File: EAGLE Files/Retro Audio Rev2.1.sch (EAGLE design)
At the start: 72 parts, among them IC1 MAX98357A, Q1 2.5A/30V, Q2 MBT3904DW1T1, Q3 AOD417, SW1 OS102011MA1Q, SW5 PEC11, U2 ESP-WROOM-32, U3 AP2112K-3.3V, U4 FT231XS, X2 19269

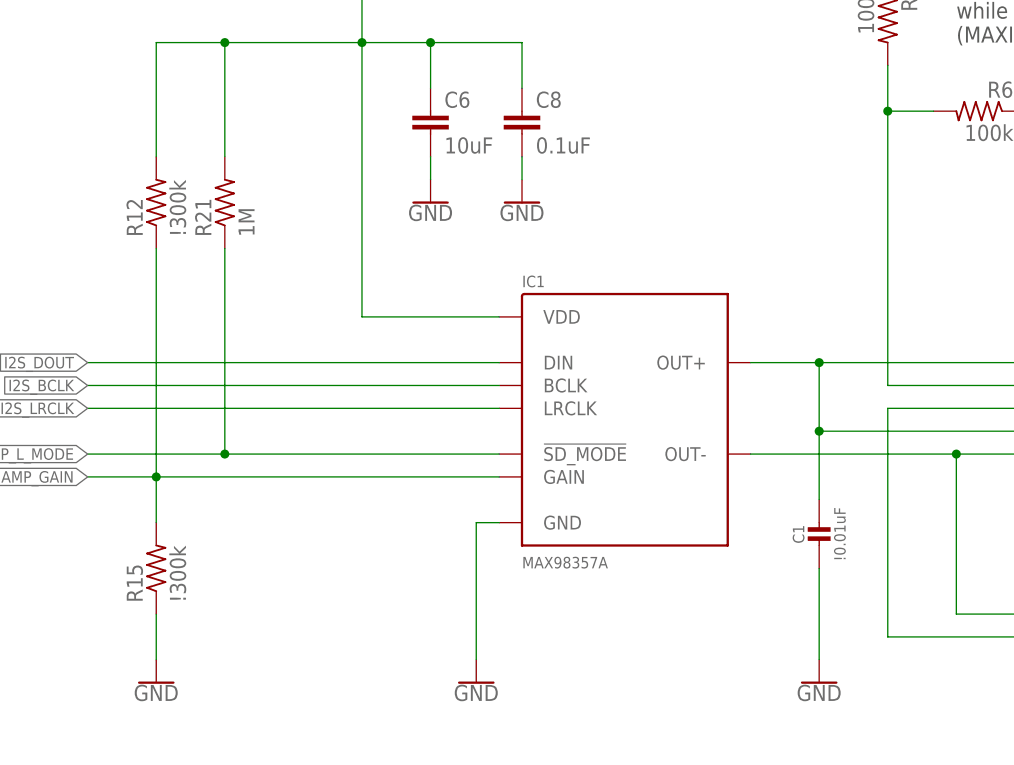
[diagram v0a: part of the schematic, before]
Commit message: Updated to show unused parts
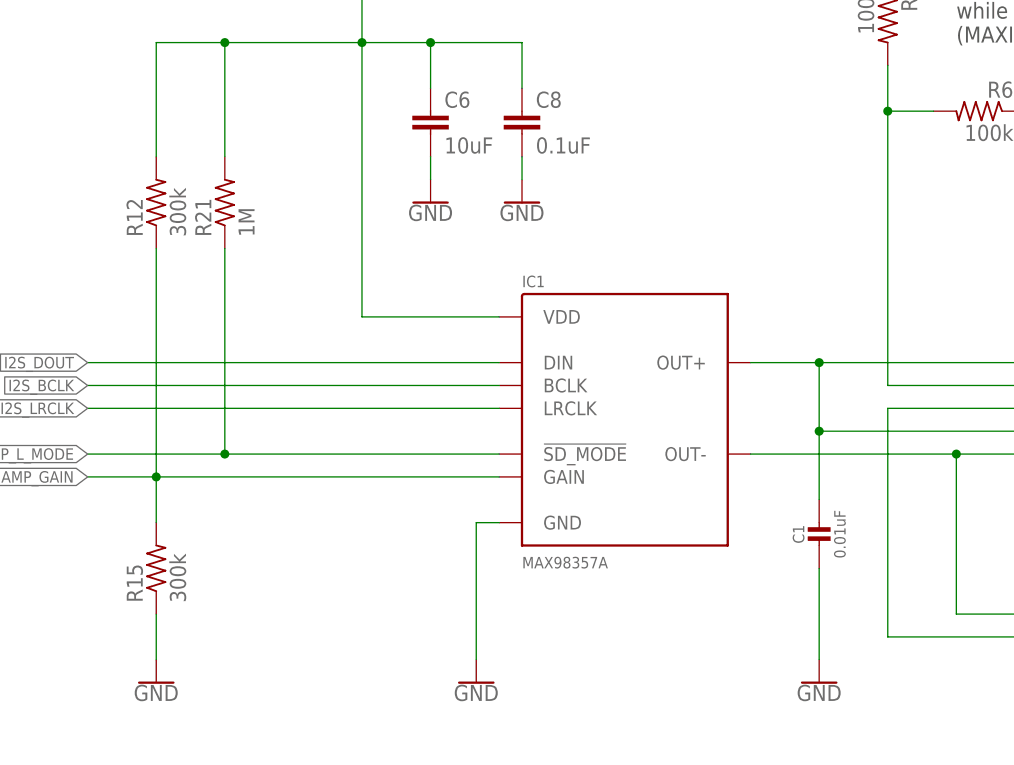
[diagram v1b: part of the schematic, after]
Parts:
- C1: value \!0.01uF -> 0.01uF
- R12, R15: value \!300k -> 300k
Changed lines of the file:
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@@
 </attributes>
 <variantdefs>
+<variantdef name="Standard" current="yes"/>
 </variantdefs>
 <classes>
@@
 <part name="X2" library="microbuilder" deviceset="AUDIO_3.5MMJACK" device="" value="19269"/>
 <part name="SUPPLY1" library="SparkFun-PowerSymbols" deviceset="3.3V" device=""/>
-<part name="C1" library="microbuilder" deviceset="CAP_CERAMIC" device="0603_NO" value="\!0.01uF"/>
+<part name="C1" library="microbuilder" deviceset="CAP_CERAMIC" device="0603_NO" value="0.01uF">
+<variant name="Standard" populate="no"/>
+</part>
 <part name="GND1" library="SparkFun-PowerSymbols" deviceset="GND" device=""/>
 <part name="SW1" library="adafruit" deviceset="OS102011MA1Q" device=""/>
@@
 <part name="GND15" library="SparkFun-PowerSymbols" deviceset="GND" device=""/>
 <part name="R21" library="adafruit" deviceset="R-US_" device="R0603" value="1M"/>
-<part name="R12" library="adafruit" deviceset="R-US_" device="R0603" value="\!300k"/>
-<part name="R15" library="adafruit" deviceset="R-US_" device="R0603" value="\!300k"/>
+<part name="R12" library="adafruit" deviceset="R-US_" device="R0603" value="300k">
+<variant name="Standard" populate="no"/>
+</part>
+<part name="R15" library="adafruit" deviceset="R-US_" device="R0603" value="300k">
+<variant name="Standard" populate="no"/>
+</part>
 <part name="GND18" library="SparkFun-PowerSymbols" deviceset="GND" device=""/>
 <part name="Q3" library="microbuilder" deviceset="MOSFET-P" device="TO252" value="AOD417"/>
